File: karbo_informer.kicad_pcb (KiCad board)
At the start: 2 copper layers, 12 parts, among them IC1 MAX7219, IC2 MAX7219, P1 USB_OTG

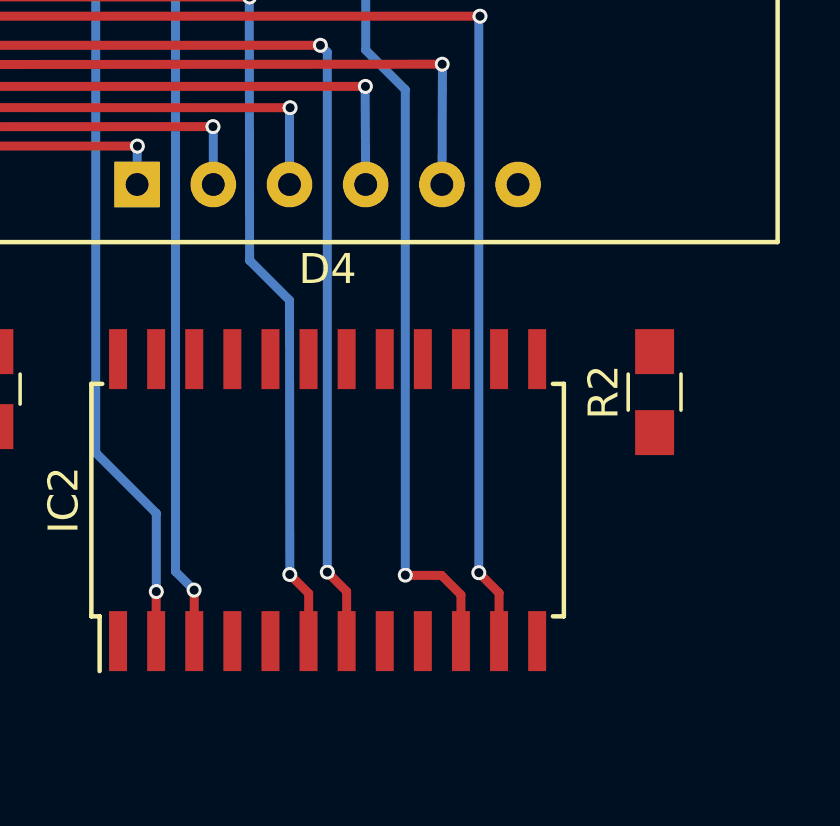
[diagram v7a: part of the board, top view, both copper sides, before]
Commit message: Wire for DIG_7 to MAX7219 in the sell line
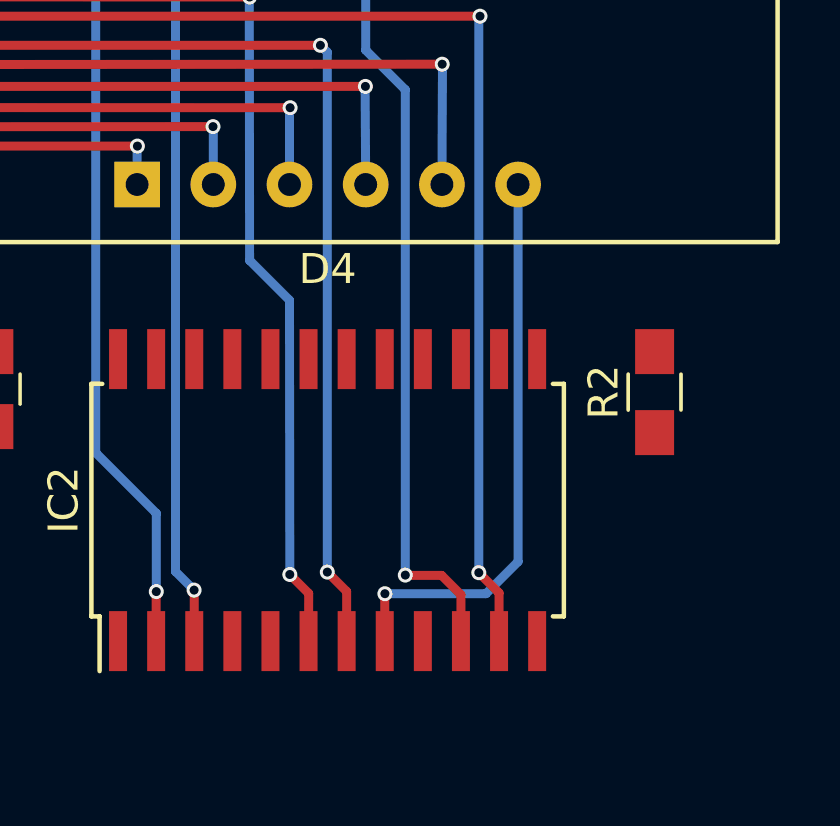
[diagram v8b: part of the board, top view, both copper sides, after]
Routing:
- net /S_DIG_7: track 0.00 -> 19.0 mm, vias 0 -> 1
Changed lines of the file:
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@@
   (general
     (links 69)
-    (no_connects 31)
+    (no_connects 30)
     (area 23.915 20.025 86.425001 77.825001)
     (thickness 1.6)
     (drawings 0)
-    (tracks 321)
+    (tracks 327)
     (zones 0)
     (modules 12)
@@
   (segment (start 77.45 29.33) (end 77.44 29.34) (width 0.3) (layer F.Cu) (net 33))
   (via (at 77.45 29.33) (size 0.5) (drill 0.3) (layers F.Cu B.Cu) (net 33))
+  (segment (start 77.45 48.28) (end 77.45 60.85) (width 0.3) (layer B.Cu) (net 39) (status 400000))
+  (segment (start 73.005 61.925) (end 73.005 63.5) (width 0.3) (layer F.Cu) (net 39) (status 800000))
+  (segment (start 73.01 61.92) (end 73.005 61.925) (width 0.3) (layer F.Cu) (net 39))
+  (via (at 73.01 61.92) (size 0.5) (drill 0.3) (layers F.Cu B.Cu) (net 39))
+  (segment (start 76.38 61.92) (end 73.01 61.92) (width 0.3) (layer B.Cu) (net 39))
+  (segment (start 77.45 60.85) (end 76.38 61.92) (width 0.3) (layer B.Cu) (net 39))
 )
